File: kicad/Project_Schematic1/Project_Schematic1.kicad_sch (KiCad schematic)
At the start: 42 parts, among them M1 Flag_Servo, M2 Motor_Left, M3 Motor_Bottom, M4 Motor_Right, Q1 NPN, Q2 NPN, Q3 NPN, SW1 SW_Push, U1 74xxx244, U2 PIC32MX170F256B, U3 CD4052, U4 QTR-HD-01A, U5 Left_Drum_LEDs, U6 Bottom_Drum_LEDs, U7 Right_Drum_LEDs, U8 Clock_LEDs

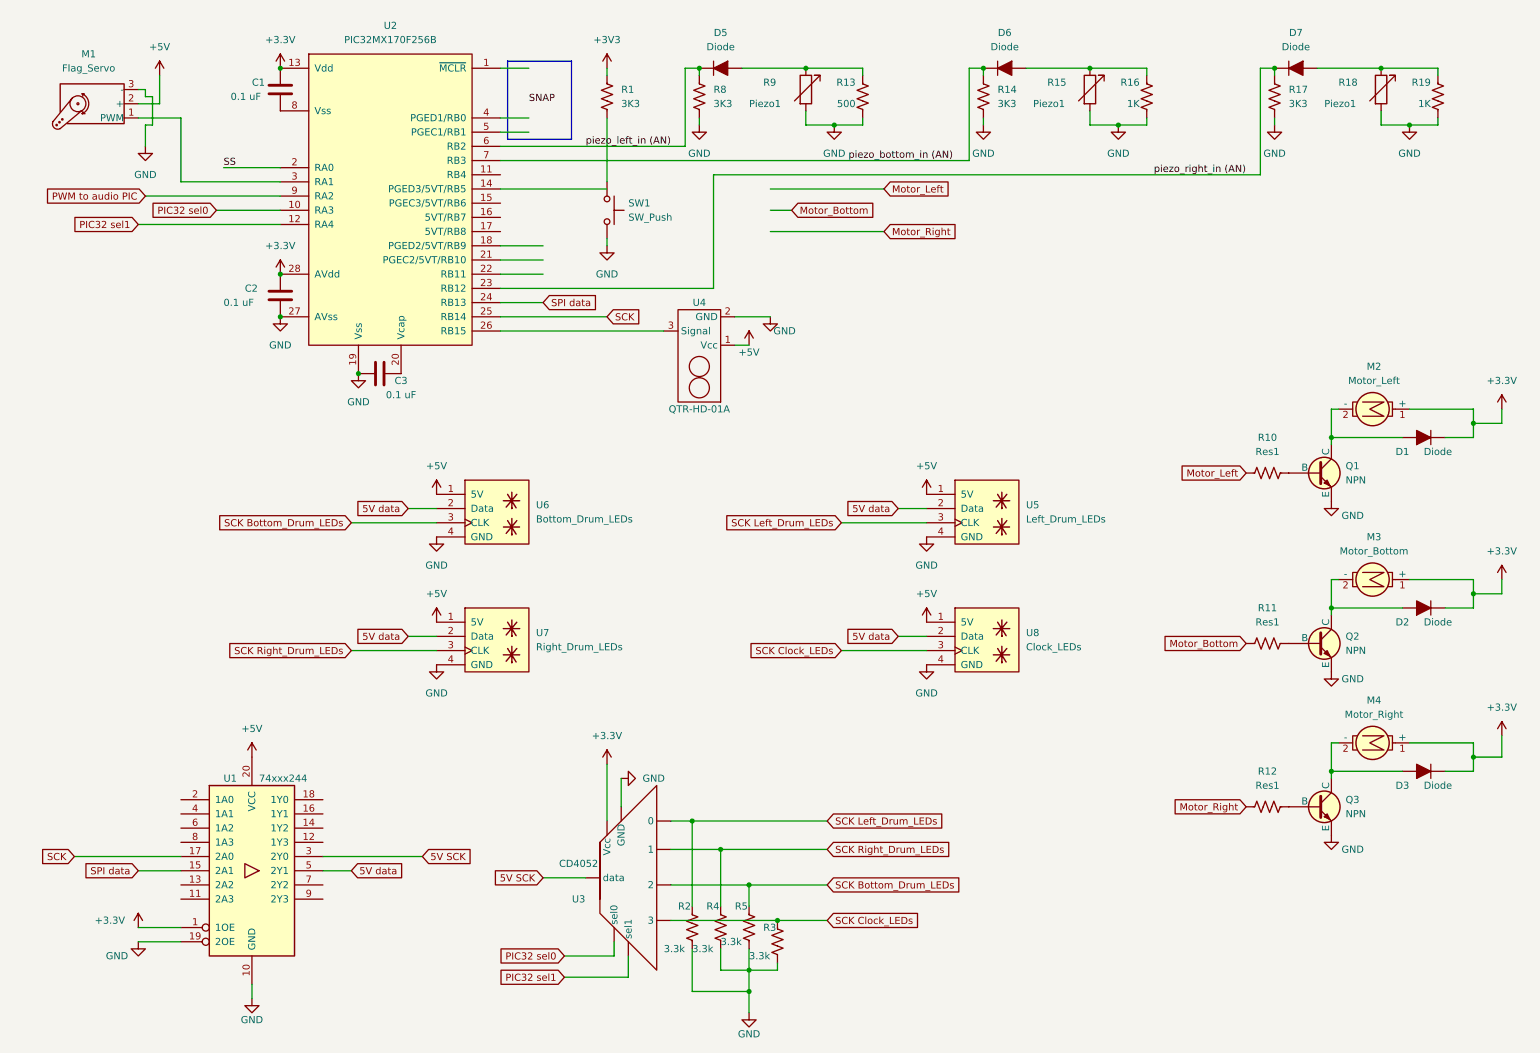
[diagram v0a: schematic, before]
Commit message: Clip piezo signal at 3.3V + Increase sensitivity with resistors on L, B drums
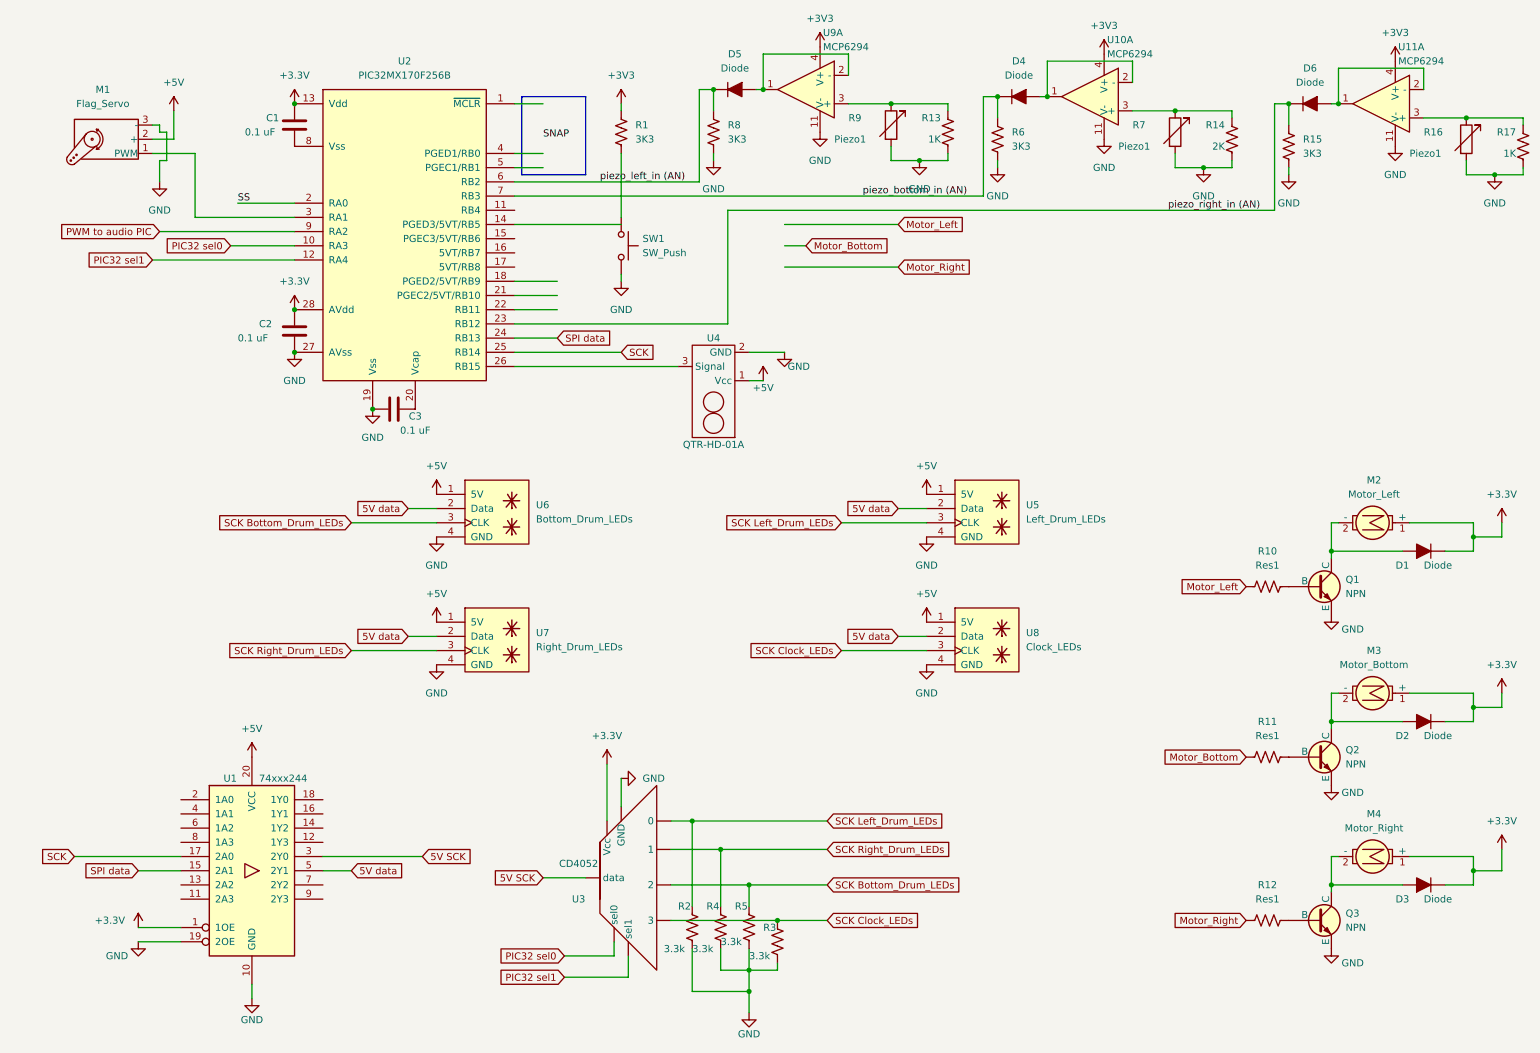
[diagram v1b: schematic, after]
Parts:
- removed D7: Diode, symbol ME218_BaseLib:Diode
- removed R15, R18: Piezo1, symbol ME218_BaseLib:Res_Adj2
- removed R16, R19: 1K, symbol ME218_BaseLib:Res1
- added D4: Diode, symbol ME218_BaseLib:Diode
- added R15, R6: 3K3, symbol ME218_BaseLib:Res1
- added R16, R7: Piezo1, symbol ME218_BaseLib:Res_Adj2
- added U10, U11, U9: MCP6294, symbol ME218_BaseLib:MCP6294
- R13: value 500 -> 1K
- R14: value 3K3 -> 2K
- R17: value 3K3 -> 1K
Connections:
- net +3V3: now also U10.4 (V+), U11.4 (V+), U9.4 (V+)
- net GND: now also R14.1, R17.1, R15.2, R16.2, R6.2, R7.2, U10.11 (V-), U11.11 (V-), U9.11 (V-); no longer R14.2, R17.2
- net piezo_bottom_in (AN): now also D4.1 (K), R6.1; no longer D6.1 (K), R14.1
- net piezo_right_in (AN): now also D6.1 (K), R15.1; no longer R17.1
- net at R13.2, R9.1: now also U9.3 (+); no longer D5.2 (A)
- net at D6.2 (A): now also U11.1, U11.2 (-)
- new net: D5.2 (A), U9.1, U9.2 (-)
- new net: R14.2, R7.1, U10.3 (+)
- new net: R16.1, R17.2, U11.3 (+)
- new net: D4.2 (A), U10.1, U10.2 (-)
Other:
- moved on the sheet: C1, C2, C3, D1, D2, D3, D5, M1, M2, M3, M4, Q1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

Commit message: Update schematic with new pins
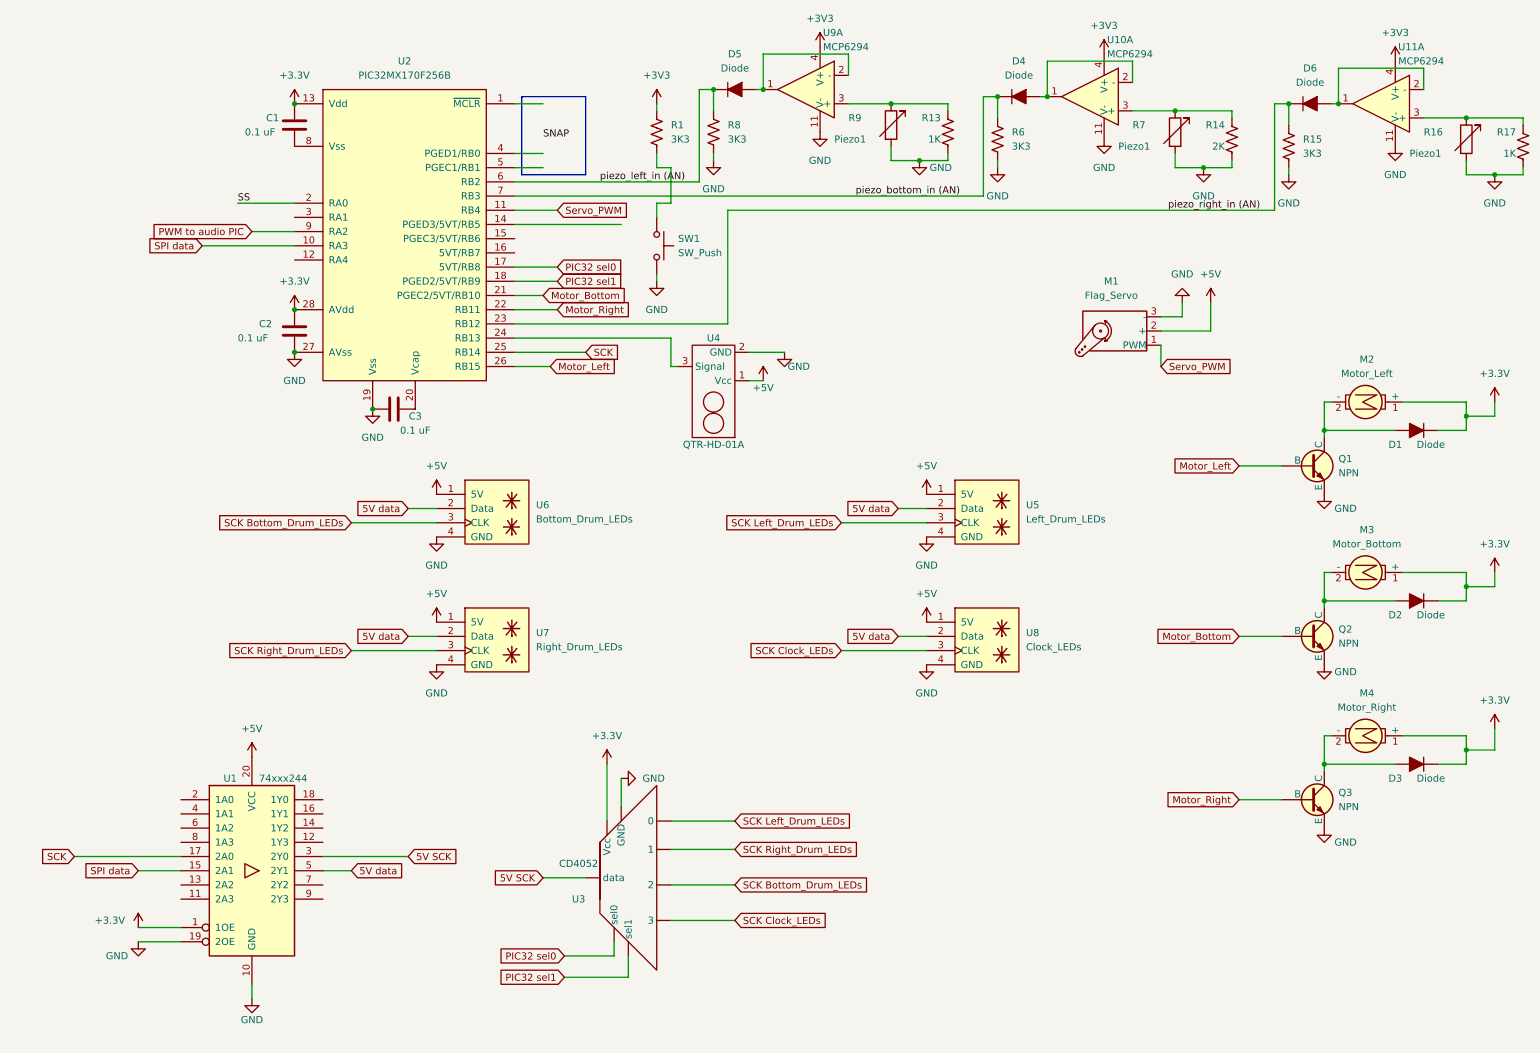
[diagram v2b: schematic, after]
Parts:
- removed R10, R11, R12: Res1, symbol ME218_BaseLib:Res1
- removed R2, R3, R4, R5: 3.3k, symbol ME218_BaseLib:Res1
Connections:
- net Motor_Bottom: now also Q2.1 (B), U2.21 (PGEC2/5VT/RB10)
- net Motor_Left: now also Q1.1 (B), U2.26 (RB15)
- net Motor_Right: now also Q3.1 (B), U2.22 (RB11)
- net PIC32 sel0: now also U2.17 (5VT/RB8); no longer U2.10 (RA3)
- net PIC32 sel1: now also U2.18 (PGED2/5VT/RB9); no longer U2.12 (RA4)
- net SPI data: now also U2.10 (RA3); no longer U2.24 (RB13)
- net Servo_PWM: now reaches U2.11 (RB4)
- net Servo_PWM: now also M1.1 (PWM)
- net at U4.3 (Signal): now also U2.24 (RB13); no longer U2.26 (RB15)
- net at U2.3 (RA1): no longer M1.1 (PWM)
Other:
- moved on the sheet: D1, D2, D3, M1, M2, M3, M4, Q1, Q2, Q3, R1, SW1

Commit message: Update KiCad with motor button and new pins for MUX sel0 and audio PWM
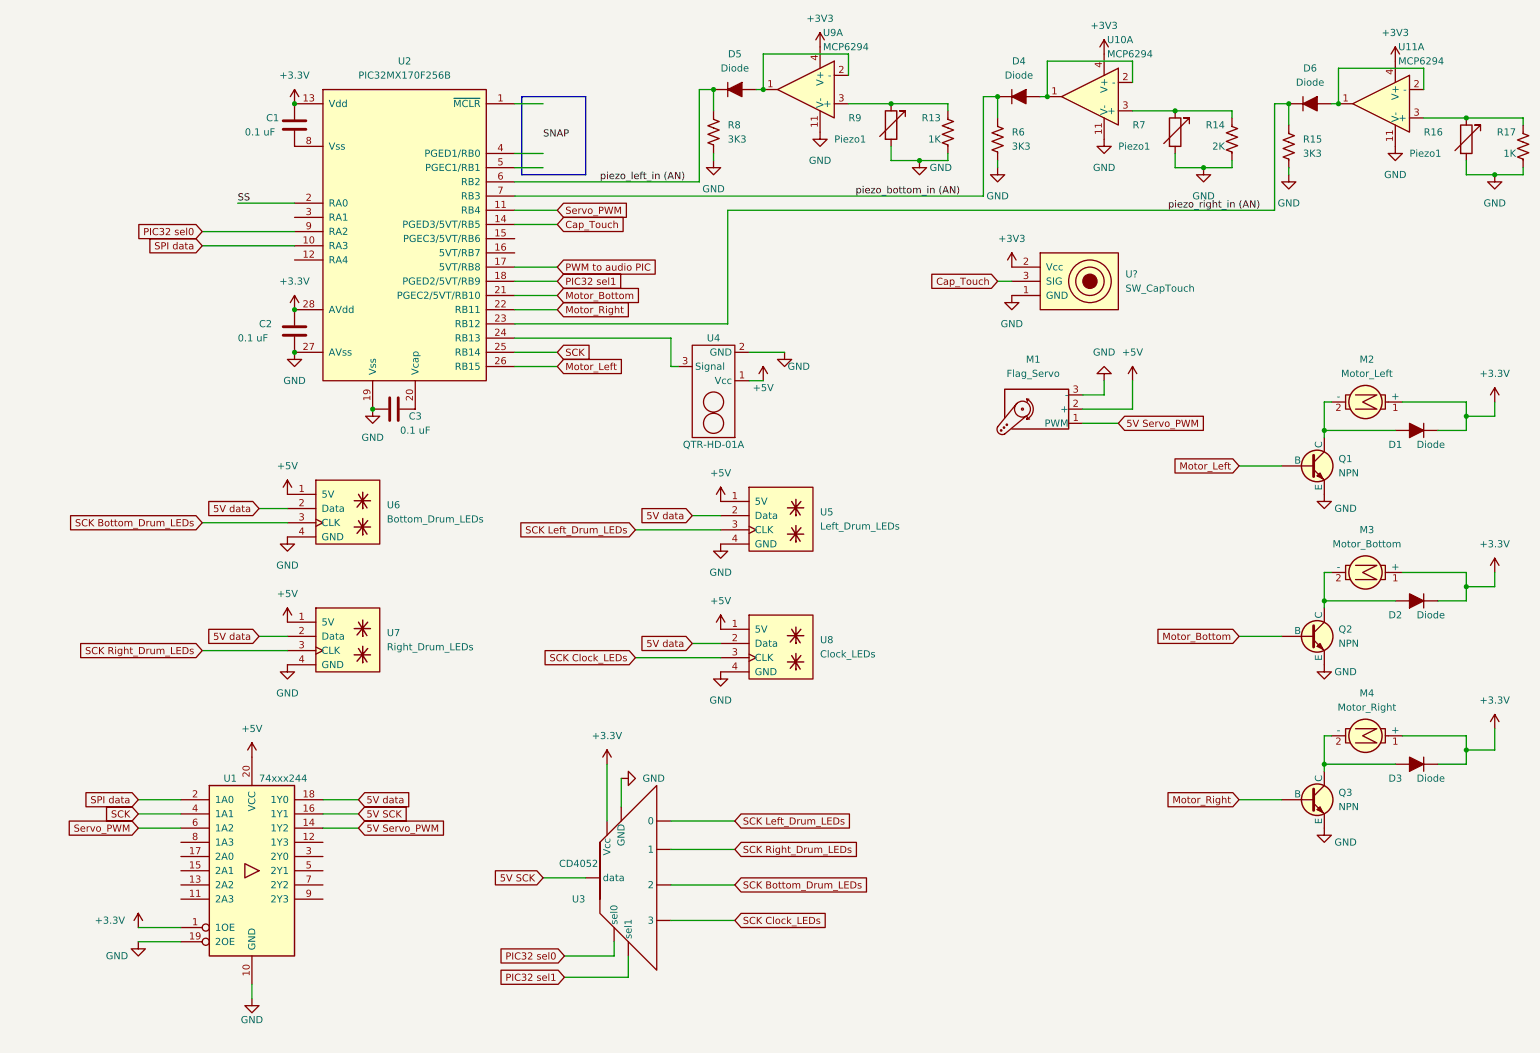
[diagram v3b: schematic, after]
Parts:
- removed R1: 3K3, symbol Device:R_US
- removed SW1: SW_Push, symbol Switch:SW_Push
- added U?: SW_CapTouch, symbol ME218_BaseLib:SW_CapTouch
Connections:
- net +3V3: now also U?.2 (Vcc)
- net 5V SCK: now also U1.16 (1Y1); no longer U1.3 (2Y0)
- net 5V data: now also U1.18 (1Y0); no longer U1.5 (2Y1)
- net GND: now also U?.1 (GND)
- net PIC32 sel0: now also U2.9 (RA2); no longer U2.17 (5VT/RB8)
- net PWM to audio PIC: now also U2.17 (5VT/RB8); no longer U2.9 (RA2)
- net SCK: now also U1.4 (1A1); no longer U1.17 (2A0)
- net SPI data: now also U1.2 (1A0); no longer U1.15 (2A1)
- net Servo_PWM: now also U1.6 (1A2); no longer M1.1 (PWM)
- net Cap_Touch: now reaches U2.14 (PGED3/5VT/RB5)
- net Cap_Touch: now also U?.3 (SIG)
- net 5V Servo_PWM: now reaches U1.14 (1Y2)
- net 5V Servo_PWM: now also M1.1 (PWM)
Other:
- moved on the sheet: M1, U5, U6, U7, U8

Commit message: Add bypass caps and update piezo resistor values in Kicad
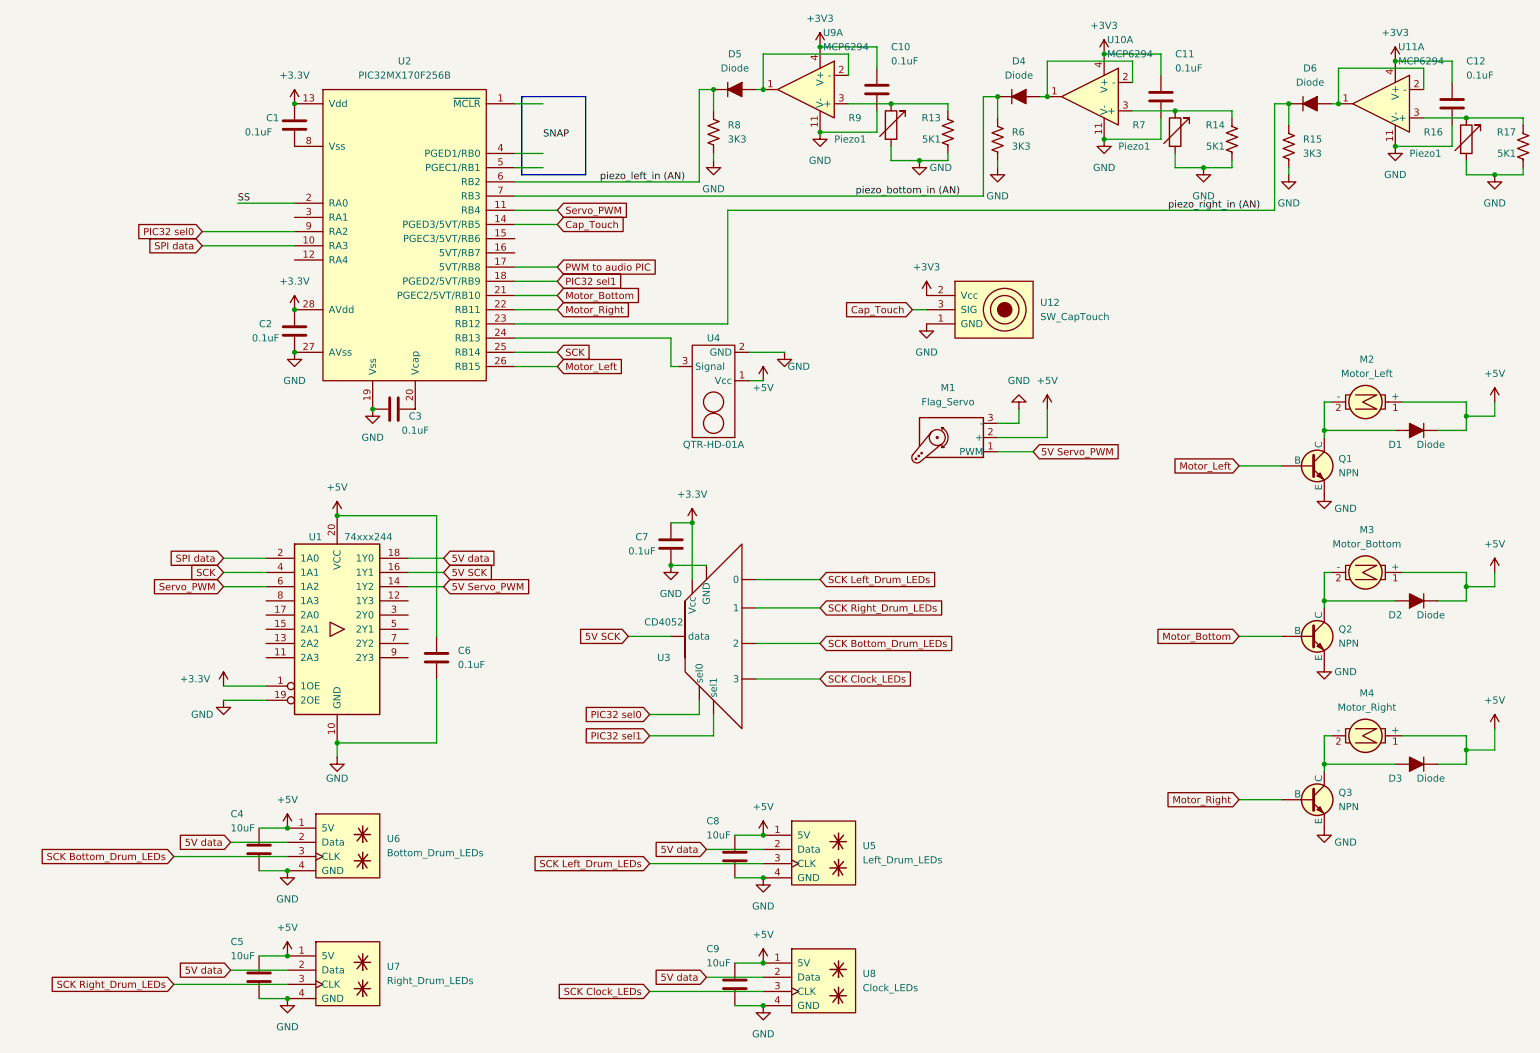
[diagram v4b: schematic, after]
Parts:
- added C10, C11, C12, C6, C7: 0.1uF, symbol ME218_BaseLib:Cap
- added C4, C5, C8, C9: 10uF, symbol ME218_BaseLib:Cap
- C1, C2, C3: value 0.1 uF -> 0.1uF
- R13, R17: value 1K -> 5K1
- R14: value 2K -> 5K1
- gave numbers to parts that had none: 1
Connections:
- net +3.3V: now also C7.1; no longer D1.1 (K), D2.1 (K), D3.1 (K), M2.1 (+), M3.1 (+), M4.1 (+)
- net +3V3: now also C10.1, C11.1, C12.1
- net +5V: now also D1.1 (K), D2.1 (K), D3.1 (K), M2.1 (+), M3.1 (+), M4.1 (+), C4.1, C5.1, C6.1, C8.1, C9.1
- net GND: now also C10.2, C11.2, C12.2, C4.2, C5.2, C6.2, C7.2, C8.2, C9.2
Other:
- moved on the sheet: M1, U1, U12, U3, U5, U6, U7, U8
